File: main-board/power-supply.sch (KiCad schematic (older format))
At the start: 25 parts, among them P3 IEC60320 C7, Q1 Q_NMOS_DGS, U2 AME40-12SMAZ, U3 ROM1205S, U4 AMS1117

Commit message: Zewnetrzny zasilacz 12V
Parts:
- removed C12, C13: 680n, symbol C
- removed F1: F_Small, symbol F_Small
- removed L2: 33mH, symbol DTSN-12/33/0.9
- removed P3: IEC60320 C7, symbol CONN_01X02
- removed U2: AME40-12SMAZ, symbol AME40-12SMAZ
- added P?: CONN_01X03, symbol CONN_01X03
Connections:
- wire segments 63 -> 54
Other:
- moved on the sheet: C1, C14, C15, C16, C17, C2, C?, D2, D3, L4, L?, Q1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

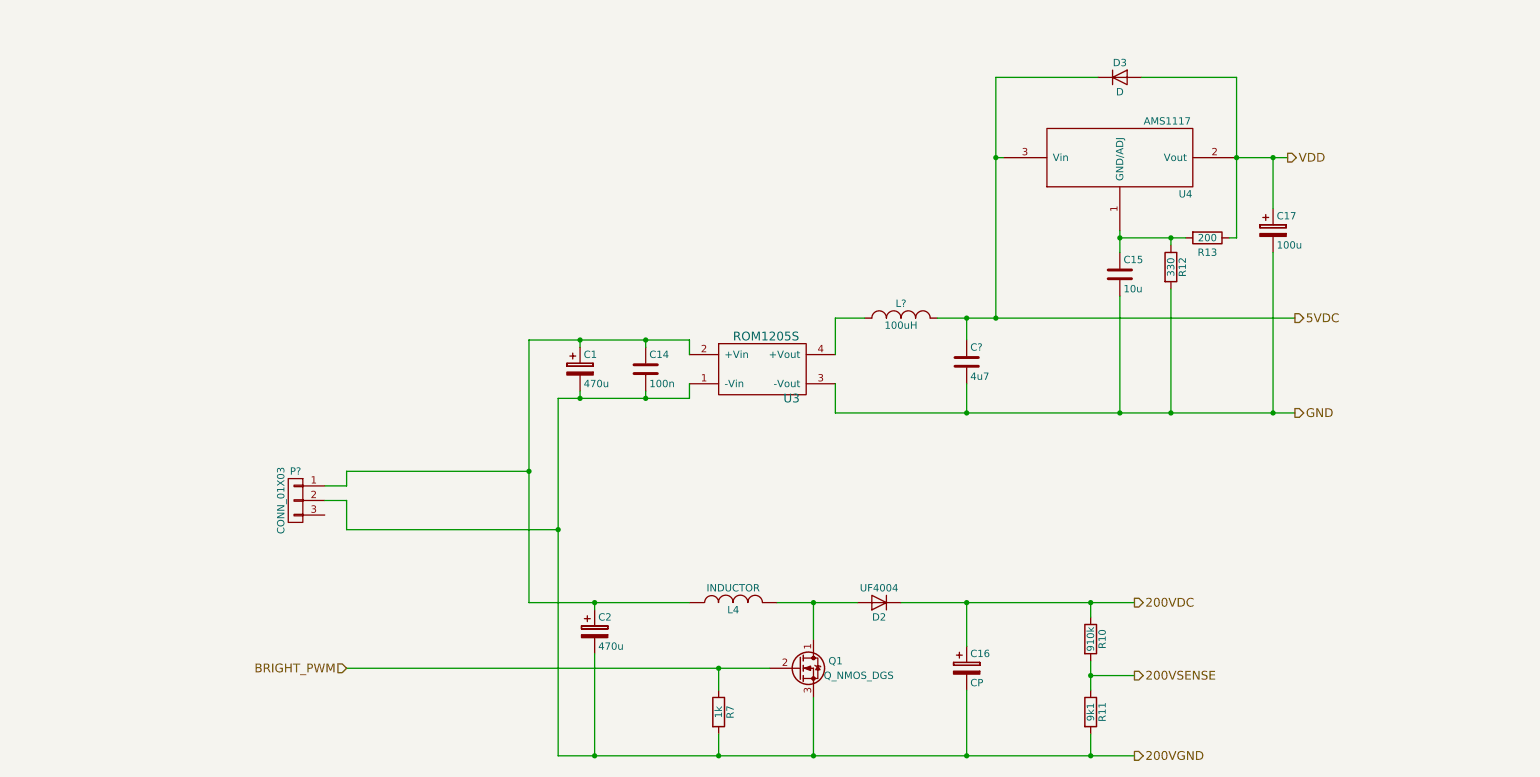
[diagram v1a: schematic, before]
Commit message: Oznaczenie MOSFET-ow od I2C; pojemnosc do filtrowania wysokich czestotliwosci za przetwornica boost; obudowy wiekszosci elementow
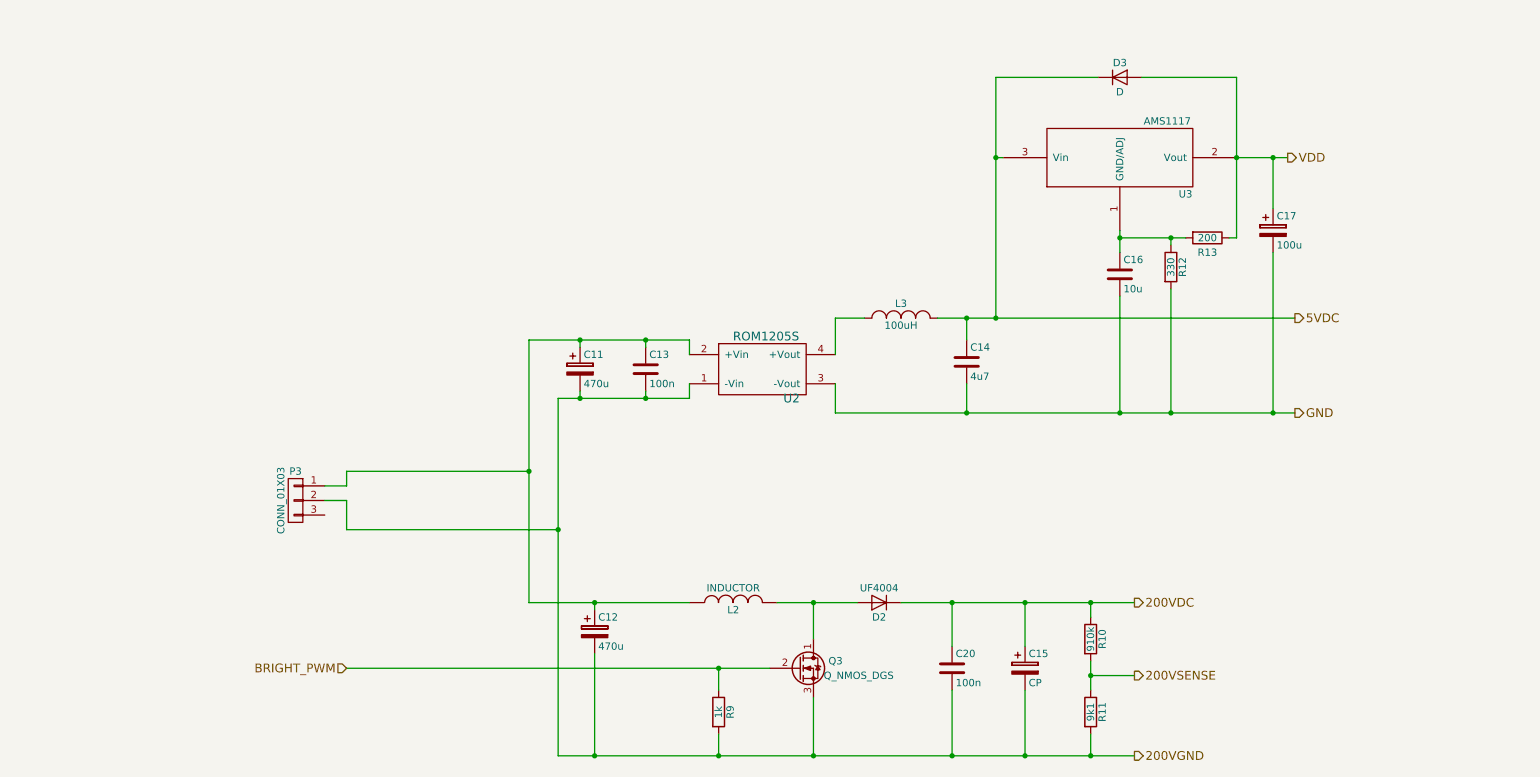
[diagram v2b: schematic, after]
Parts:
- added C20: 100n, Capacitors_SMD:C_1206_HandSoldering, symbol C
- C11: renamed from C1; footprint (none) -> Capacitors_SMD:c_elec_10x10
- C12: renamed from C2; footprint (none) -> Capacitors_SMD:c_elec_10x10
- C13: renamed from C14; footprint (none) -> Capacitors_SMD:C_0805_HandSoldering
- C14: renamed from C?; footprint (none) -> Capacitors_SMD:C_0805_HandSoldering
- C15: renamed from C16; footprint (none) -> Capacitors_SMD:c_elec_6.3x5.7
- C16: renamed from C15; footprint (none) -> Capacitors_Tantalum_SMD:TantalC_SizeB_EIA-3528_HandSoldering
- C17: footprint (none) -> Capacitors_Tantalum_SMD:TantalC_SizeC_EIA-6032_HandSoldering
- D2: footprint (none) -> Diodes_ThroughHole:Diode_DO-41_SOD81_Horizontal_RM10
- D3: footprint (none) -> Diodes_SMD:MiniMELF_Handsoldering
- P3: renamed from P?; footprint (none) -> Connect:BARREL_JACK
- R10, R11: footprint (none) -> Resistors_SMD:R_1206_HandSoldering
- R12, R13: footprint (none) -> Resistors_SMD:R_0805_HandSoldering
- R9: renamed from R7; footprint (none) -> Resistors_SMD:R_0805_HandSoldering
- U3: renamed from U4; footprint (none) -> TO_SOT_Packages_SMD:TO-252-2Lead
- gave numbers to parts that had none: 1
- renumbered L4 to L2, Q1 to Q3, U3 to U2
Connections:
- net 200VDC: now also C20.1
- net 200VGND: now also C20.2
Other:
- moved on the sheet: C15
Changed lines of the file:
@@
 	4250 3300 4250 5750
 $Comp
-L INDUCTOR L4
+L INDUCTOR L2
 U 1 1 581538C6
 P 5450 4700
-F 0 "L4" V 5400 4700 50  0000 C CNN
+F 0 "L2" V 5400 4700 50  0000 C CNN
 F 1 "INDUCTOR" V 5550 4700 50  0000 C CNN
-F 2 "" H 5450 4700 50  0000 C CNN
+F 2 "" H 5450 4700 50  0001 C CNN
 F 3 "" H 5450 4700 50  0000 C CNN
 	1    5450 4700
@@
 $EndComp
 $Comp
-L Q_NMOS_DGS Q1
+L Q_NMOS_DGS Q3
 U 1 1 581540AF
 P 5900 5150
-F 0 "Q1" H 6200 5200 50  0000 R CNN
+F 0 "Q3" H 6200 5200 50  0000 R CNN
 F 1 "Q_NMOS_DGS" H 6550 5100 50  0000 R CNN
-F 2 "" H 6100 5250 50  0000 C CNN
+F 2 "" H 6100 5250 50  0001 C CNN
 F 3 "" H 5900 5150 50  0000 C CNN
 	1    5900 5150
@@
 F 0 "D2" H 6450 4800 50  0000 C CNN
 F 1 "UF4004" H 6450 4600 50  0000 C CNN
-F 2 "" H 6450 4700 50  0000 C CNN
+F 2 "Diodes_ThroughHole:Diode_DO-41_SOD81_Horizontal_RM10" H 6450 4700 50  0001 C CNN
 F 3 "http://www.vishay.com/docs/88755/uf4001.pdf" H 6450 4700 50  0001 C CNN
 	1    6450 4700
@@
 $EndComp
 $Comp
-L CP C16
+L CP C15
 U 1 1 58154567
-P 7050 5150
-F 0 "C16" H 7075 5250 50  0000 L CNN
-F 1 "CP" H 7075 5050 50  0000 L CNN
-F 2 "" H 7088 5000 50  0000 C CNN
-F 3 "" H 7050 5150 50  0000 C CNN
-	1    7050 5150
+P 7450 5150
+F 0 "C15" H 7475 5250 50  0000 L CNN
+F 1 "CP" H 7475 5050 50  0000 L CNN
+F 2 "Capacitors_SMD:c_elec_6.3x5.7" H 7488 5000 50  0001 C CNN
+F 3 "" H 7450 5150 50  0000 C CNN
+	1    7450 5150
 	1    0    0    -1
 $EndComp
@@
 	6600 4700 8200 4700
 Wire Wire Line
-	7050 4700 7050 5000
-Connection ~ 7050 4700
+	7450 4700 7450 5000
+Connection ~ 7450 4700
 Connection ~ 4050 3800
 Wire Wire Line
@@
 	4250 5750 8200 5750
 Wire Wire Line
-	7050 5750 7050 5300
-Connection ~ 7050 5750
+	7450 5750 7450 5300
+Connection ~ 7450 5750
 Connection ~ 6000 5750
 Connection ~ 4250 4200
@@
 F 0 "R10" V 7980 4950 50  0000 C CNN
 F 1 "910k" V 7900 4950 50  0000 C CNN
-F 2 "" V 7830 4950 50  0000 C CNN
+F 2 "Resistors_SMD:R_1206_HandSoldering" V 7830 4950 50  0001 C CNN
 F 3 "" H 7900 4950 50  0000 C CNN
 F 4 "1%" V 7900 4950 60  0001 C CNN "Dokładność"
@@
 F 0 "R11" V 7980 5450 50  0000 C CNN
 F 1 "9k1" V 7900 5450 50  0000 C CNN
-F 2 "" V 7830 5450 50  0000 C CNN
+F 2 "Resistors_SMD:R_1206_HandSoldering" V 7830 5450 50  0001 C CNN
 F 3 "" H 7900 5450 50  0000 C CNN
 F 4 "1%" V 7900 5450 60  0001 C CNN "Dokładność"
@@
 Connection ~ 7900 5200
 $Comp
-L R R7
+L R R9
 U 1 1 582BEA4B
 P 5350 5450
-F 0 "R7" V 5430 5450 50  0000 C CNN
+F 0 "R9" V 5430 5450 50  0000 C CNN
 F 1 "1k" V 5350 5450 50  0000 C CNN
-F 2 "" V 5280 5450 50  0000 C CNN
+F 2 "Resistors_SMD:R_0805_HandSoldering" V 5280 5450 50  0001 C CNN
 F 3 "" H 5350 5450 50  0000 C CNN
 	1    5350 5450
@@
 Connection ~ 5350 5750
 $Comp
-L ROM1205S U3
+L ROM1205S U2
 U 1 1 582656C6
 P 5650 3100
-F 0 "U3" H 5850 2900 60  0000 C CNN
+F 0 "U2" H 5850 2900 60  0000 C CNN
 F 1 "ROM1205S" H 5675 3325 60  0000 C CNN
 F 2 "" H 5550 3125 60  0001 C CNN
@@
 	5150 2900 5150 3000
 $Comp
-L C C14
+L C C13
 U 1 1 582658FD
 P 4850 3100
-F 0 "C14" H 4875 3200 50  0000 L CNN
+F 0 "C13" H 4875 3200 50  0000 L CNN
 F 1 "100n" H 4875 3000 50  0000 L CNN
-F 2 "" H 4888 2950 50  0000 C CNN
+F 2 "Capacitors_SMD:C_0805_HandSoldering" H 4888 2950 50  0001 C CNN
 F 3 "" H 4850 3100 50  0000 C CNN
 	1    4850 3100
@@
 F 0 "D3" H 8100 1200 50  0000 C CNN
 F 1 "D" H 8100 1000 50  0000 C CNN
-F 2 "" H 8100 1100 50  0000 C CNN
+F 2 "Diodes_SMD:MiniMELF_Handsoldering" H 8100 1100 50  0001 C CNN
 F 3 "" H 8100 1100 50  0000 C CNN
 	1    8100 1100
@@
 	7250 1100 7950 1100
 $Comp
-L AMS1117 U4
+L AMS1117 U3
 U 1 1 582722A0
 P 8100 1650
-F 0 "U4" H 8550 1400 50  0000 C CNN
+F 0 "U3" H 8550 1400 50  0000 C CNN
 F 1 "AMS1117" H 8425 1900 50  0000 C CNN
-F 2 "" H 8100 1650 60  0001 C CNN
+F 2 "TO_SOT_Packages_SMD:TO-252-2Lead" H 8100 1650 60  0001 C CNN
 F 3 "" H 8100 1650 60  0001 C CNN
 	1    8100 1650
@@
 F 0 "C17" H 9175 2250 50  0000 L CNN
 F 1 "100u" H 9175 2050 50  0000 L CNN
-F 2 "" H 9188 2000 50  0000 C CNN
+F 2 "Capacitors_Tantalum_SMD:TantalC_SizeC_EIA-6032_HandSoldering" H 9188 2000 50  0001 C CNN
 F 3 "" H 9150 2150 50  0000 C CNN
 	1    9150 2150
@@
 F 0 "R13" V 8800 2200 50  0000 C CNN
 F 1 "200" V 8700 2200 50  0000 C CNN
-F 2 "" V 8630 2200 50  0000 C CNN
+F 2 "Resistors_SMD:R_0805_HandSoldering" V 8630 2200 50  0001 C CNN
 F 3 "" H 8700 2200 50  0000 C CNN
 	1    8700 2200
@@
 F 0 "R12" V 8530 2400 50  0000 C CNN
 F 1 "330" V 8450 2400 50  0000 C CNN
-F 2 "" V 8380 2400 50  0000 C CNN
+F 2 "Resistors_SMD:R_0805_HandSoldering" V 8380 2400 50  0001 C CNN
 F 3 "" H 8450 2400 50  0000 C CNN
 	1    8450 2400
@@
 $EndComp
 $Comp
-L C C15
+L C C16
 U 1 1 58273455
 P 8100 2450
-F 0 "C15" H 8125 2550 50  0000 L CNN
+F 0 "C16" H 8125 2550 50  0000 L CNN
 F 1 "10u" H 8125 2350 50  0000 L CNN
-F 2 "" H 8138 2300 50  0000 C CNN
+F 2 "Capacitors_Tantalum_SMD:TantalC_SizeB_EIA-3528_HandSoldering" H 8138 2300 50  0001 C CNN
 F 3 "" H 8100 2450 50  0000 C CNN
 	1    8100 2450
@@
 Connection ~ 9150 3400
 $Comp
-L CP C1
+L CP C11
 U 1 1 582F7B7F
 P 4400 3100
-F 0 "C1" H 4425 3200 50  0000 L CNN
+F 0 "C11" H 4425 3200 50  0000 L CNN
 F 1 "470u" H 4425 3000 50  0000 L CNN
-F 2 "" H 4438 2950 50  0000 C CNN
+F 2 "Capacitors_SMD:c_elec_10x10" H 4438 2950 50  0001 C CNN
 F 3 "" H 4400 3100 50  0000 C CNN
 F 4 "Tantalowe" H 4400 3100 60  0001 C CNN "Rodzaj"
@@
 Connection ~ 4400 3300
 $Comp
-L CP C2
+L CP C12
 U 1 1 582F81ED
 P 4500 4900
-F 0 "C2" H 4525 5000 50  0000 L CNN
+F 0 "C12" H 4525 5000 50  0000 L CNN
 F 1 "470u" H 4525 4800 50  0000 L CNN
-F 2 "" H 4538 4750 50  0000 C CNN
+F 2 "Capacitors_SMD:c_elec_10x10" H 4538 4750 50  0001 C CNN
 F 3 "" H 4500 4900 50  0000 C CNN
 F 4 "Tantalowe" H 4500 4900 60  0001 C CNN "Rodzaj"
@@
 Connection ~ 4500 5750
 $Comp
-L INDUCTOR_SMALL L?
+L INDUCTOR_SMALL L3
 U 1 1 582FA66C
 P 6600 2750
-F 0 "L?" H 6600 2850 50  0000 C CNN
+F 0 "L3" H 6600 2850 50  0000 C CNN
 F 1 "100uH" H 6600 2700 50  0000 C CNN
-F 2 "" H 6600 2750 50  0000 C CNN
+F 2 "" H 6600 2750 50  0001 C CNN
 F 3 "" H 6600 2750 50  0000 C CNN
 	1    6600 2750
@@
 $EndComp
 $Comp
-L C C?
+L C C14
 U 1 1 582FAA04
 P 7050 3050
-F 0 "C?" H 7075 3150 50  0000 L CNN
+F 0 "C14" H 7075 3150 50  0000 L CNN
 F 1 "4u7" H 7075 2950 50  0000 L CNN
-F 2 "" H 7088 2900 50  0000 C CNN
+F 2 "Capacitors_SMD:C_0805_HandSoldering" H 7088 2900 50  0001 C CNN
 F 3 "" H 7050 3050 50  0000 C CNN
 	1    7050 3050
@@
 Connection ~ 7050 3400
 $Comp
-L CONN_01X03 P?
+L CONN_01X03 P3
 U 1 1 5832F9D1
 P 2450 4000
-F 0 "P?" H 2450 4200 50  0000 C CNN
+F 0 "P3" H 2450 4200 50  0000 C CNN
 F 1 "CONN_01X03" V 2550 4000 50  0000 C CNN
-F 2 "" H 2450 4000 50  0000 C CNN
+F 2 "Connect:BARREL_JACK" H 2450 4000 50  0001 C CNN
 F 3 "" H 2450 4000 50  0000 C CNN
 	1    2450 4000
@@
 Wire Wire Line
 	2800 4000 2800 4200
+$Comp
+L C C20
+U 1 1 5838FF4A
+P 6950 5150
+F 0 "C20" H 6975 5250 50  0000 L CNN
+F 1 "100n" H 6975 5050 50  0000 L CNN
+F 2 "Capacitors_SMD:C_1206_HandSoldering" H 6988 5000 50  0001 C CNN
+F 3 "" H 6950 5150 50  0000 C CNN
+	1    6950 5150
+	1    0    0    -1
+$EndComp
+Wire Wire Line
+	6950 5000 6950 4700
+Connection ~ 6950 4700
+Wire Wire Line
+	6950 5300 6950 5750
+Connection ~ 6950 5750
 $EndSCHEMATC

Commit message: Dobranie parametrow przetwornicy boost + obudowy; obudowa do dlawika z ROM1205S
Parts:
- C15: value CP -> 10u; footprint Capacitors_SMD:c_elec_6.3x5.7 -> Capacitors_ThroughHole:C_Axial_D13_L31_P38; Part no. (none) -> TVX2F100MCD
- L2: value INDUCTOR -> 10mH; footprint (none) -> Choke_Axial_ThroughHole:Choke_Horizontal_RM25mm; Part no. (none) -> 5900-103-RC
- L3: footprint (none) -> Resistors_SMD:R_1812_HandSoldering
- Q3: value Q_NMOS_DGS -> BSP324; footprint (none) -> TO_SOT_Packages_SMD:SOT-223; Part no. (none) -> BSP324H6327XTSA1
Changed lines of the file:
@@
 P 5450 4700
 F 0 "L2" V 5400 4700 50  0000 C CNN
-F 1 "INDUCTOR" V 5550 4700 50  0000 C CNN
-F 2 "" H 5450 4700 50  0001 C CNN
+F 1 "10mH" V 5550 4700 50  0000 C CNN
+F 2 "Choke_Axial_ThroughHole:Choke_Horizontal_RM25mm" H 5450 4700 50  0001 C CNN
 F 3 "" H 5450 4700 50  0000 C CNN
+F 4 "5900-103-RC" V 5450 4700 60  0001 C CNN "Part no."
 	1    5450 4700
 	0    -1   -1   0
@@
 P 5900 5150
 F 0 "Q3" H 6200 5200 50  0000 R CNN
-F 1 "Q_NMOS_DGS" H 6550 5100 50  0000 R CNN
-F 2 "" H 6100 5250 50  0001 C CNN
+F 1 "BSP324" H 5900 5350 50  0000 R CNN
+F 2 "TO_SOT_Packages_SMD:SOT-223" H 6100 5250 50  0001 C CNN
 F 3 "" H 5900 5150 50  0000 C CNN
+F 4 "BSP324H6327XTSA1" H 5900 5150 60  0001 C CNN "Part no."
 	1    5900 5150
 	1    0    0    -1
@@
 P 7450 5150
 F 0 "C15" H 7475 5250 50  0000 L CNN
-F 1 "CP" H 7475 5050 50  0000 L CNN
-F 2 "Capacitors_SMD:c_elec_6.3x5.7" H 7488 5000 50  0001 C CNN
+F 1 "10u" H 7475 5050 50  0000 L CNN
+F 2 "Capacitors_ThroughHole:C_Axial_D13_L31_P38" H 7488 5000 50  0001 C CNN
 F 3 "" H 7450 5150 50  0000 C CNN
+F 4 "TVX2F100MCD" H 7450 5150 60  0001 C CNN "Part no."
 	1    7450 5150
 	1    0    0    -1
@@
 F 0 "L3" H 6600 2850 50  0000 C CNN
 F 1 "100uH" H 6600 2700 50  0000 C CNN
-F 2 "" H 6600 2750 50  0001 C CNN
+F 2 "Resistors_SMD:R_1812_HandSoldering" H 6600 2750 50  0001 C CNN
 F 3 "" H 6600 2750 50  0000 C CNN
 	1    6600 2750

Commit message: Obudowa SIP4 do ukladu ROM1205S; utworzenie lokalnej biblioteki footprintow
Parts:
- U2: footprint (none) -> footprint-local:SIP4
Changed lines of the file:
@@
 F 0 "U2" H 5850 2900 60  0000 C CNN
 F 1 "ROM1205S" H 5675 3325 60  0000 C CNN
-F 2 "" H 5550 3125 60  0001 C CNN
+F 2 "footprint-local:SIP4" H 5550 3125 60  0001 C CNN
 F 3 "http://www.recom-power.com/pdf/Econoline/ROM.pdf" H 5550 3125 60  0001 C CNN
 	1    5650 3100

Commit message: Poprawione polaczenie sciezek; zmiana nazwy wyjscia VDD
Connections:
- net VDD renamed VDDOUT
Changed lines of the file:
@@
 	4050 4700 5150 4700
 Text HLabel 9250 1650 2    60   Output ~ 0
-VDD
+VDDOUT
 Text HLabel 9300 3400 2    60   Output ~ 0
 GND

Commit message: usunięcie błędnego połączenia VDD z +5V
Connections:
- no-connect marks 0 -> 1
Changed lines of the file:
@@
 	6950 5300 6950 5750
 Connection ~ 6950 5750
+NoConn ~ 2650 4100
 $EndSCHEMATC

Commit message: Obrys plytki 40% elementow
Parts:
- C15: footprint Capacitors_ThroughHole:C_Axial_D13_L31_P38 -> Capacitors_ThroughHole:C_Radial_D10_L20_P5
- C20: footprint Capacitors_SMD:C_1206_HandSoldering -> Capacitors_SMD:C_1812_HandSoldering
- D2: footprint Diodes_ThroughHole:Diode_DO-41_SOD81_Horizontal_RM10 -> Diodes_ThroughHole:Diode_DO-41_SOD81_Vertical_AnodeUp
- L2: value 10mH -> 100uH; footprint Choke_Axial_ThroughHole:Choke_Horizontal_RM25mm -> footprint-local:Neosid_Inductor_Sd8
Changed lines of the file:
@@
 P 5450 4700
 F 0 "L2" V 5400 4700 50  0000 C CNN
-F 1 "10mH" V 5550 4700 50  0000 C CNN
-F 2 "Choke_Axial_ThroughHole:Choke_Horizontal_RM25mm" H 5450 4700 50  0001 C CNN
-F 3 "" H 5450 4700 50  0000 C CNN
+F 1 "100uH" V 5550 4700 50  0000 C CNN
+F 2 "footprint-local:Neosid_Inductor_Sd8" H 5450 4700 50  0001 C CNN
+F 3 "http://www.tme.eu/pl/Document/4ff2ae81ca911b75713a1b32b7615e0b/kmp_2200r.pdf" H 5450 4700 50  0001 C CNN
 F 4 "5900-103-RC" V 5450 4700 60  0001 C CNN "Part no."
 	1    5450 4700
@@
 F 0 "D2" H 6450 4800 50  0000 C CNN
 F 1 "UF4004" H 6450 4600 50  0000 C CNN
-F 2 "Diodes_ThroughHole:Diode_DO-41_SOD81_Horizontal_RM10" H 6450 4700 50  0001 C CNN
+F 2 "Diodes_ThroughHole:Diode_DO-41_SOD81_Vertical_AnodeUp" H 6450 4700 50  0001 C CNN
 F 3 "http://www.vishay.com/docs/88755/uf4001.pdf" H 6450 4700 50  0001 C CNN
 	1    6450 4700
@@
 F 0 "C15" H 7475 5250 50  0000 L CNN
 F 1 "10u" H 7475 5050 50  0000 L CNN
-F 2 "Capacitors_ThroughHole:C_Axial_D13_L31_P38" H 7488 5000 50  0001 C CNN
+F 2 "Capacitors_ThroughHole:C_Radial_D10_L20_P5" H 7488 5000 50  0001 C CNN
 F 3 "" H 7450 5150 50  0000 C CNN
 F 4 "TVX2F100MCD" H 7450 5150 60  0001 C CNN "Part no."
@@
 F 0 "C20" H 6975 5250 50  0000 L CNN
 F 1 "100n" H 6975 5050 50  0000 L CNN
-F 2 "Capacitors_SMD:C_1206_HandSoldering" H 6988 5000 50  0001 C CNN
+F 2 "Capacitors_SMD:C_1812_HandSoldering" H 6988 5000 50  0001 C CNN
 F 3 "" H 6950 5150 50  0000 C CNN
 	1    6950 5150
